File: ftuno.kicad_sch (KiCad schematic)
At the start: 63 parts, among them CN1 AFC10-S04QCA-00, J1 USB_C_Receptacle_USB2.0_16P, J10 Conn_01x10_Socket, J11 Conn_01x08_Pin, J12 Conn_01x08_Socket, J2 Conn_02x03_Odd_Even, J3 Conn_01x08_Pin, J4 Conn_01x08_Socket, J5 Conn_02x04_Odd_Even, J6 Conn_01x06_Pin, J7 Conn_01x06_Socket, J8 Conn_01x04_Socket, J9 Conn_01x10_Pin, Q1 AO3401, Q2 BSS138PS_C5224289, Q3 BSS138PS_C5224289, SW1 SK12D07VG4, SW2 SKHMQLE010, U1 CH340C, U2 TPS54302, U3 ME6217C33M5G, U4 ATmega328P-A, X1 CSTCE16M0V53-R0

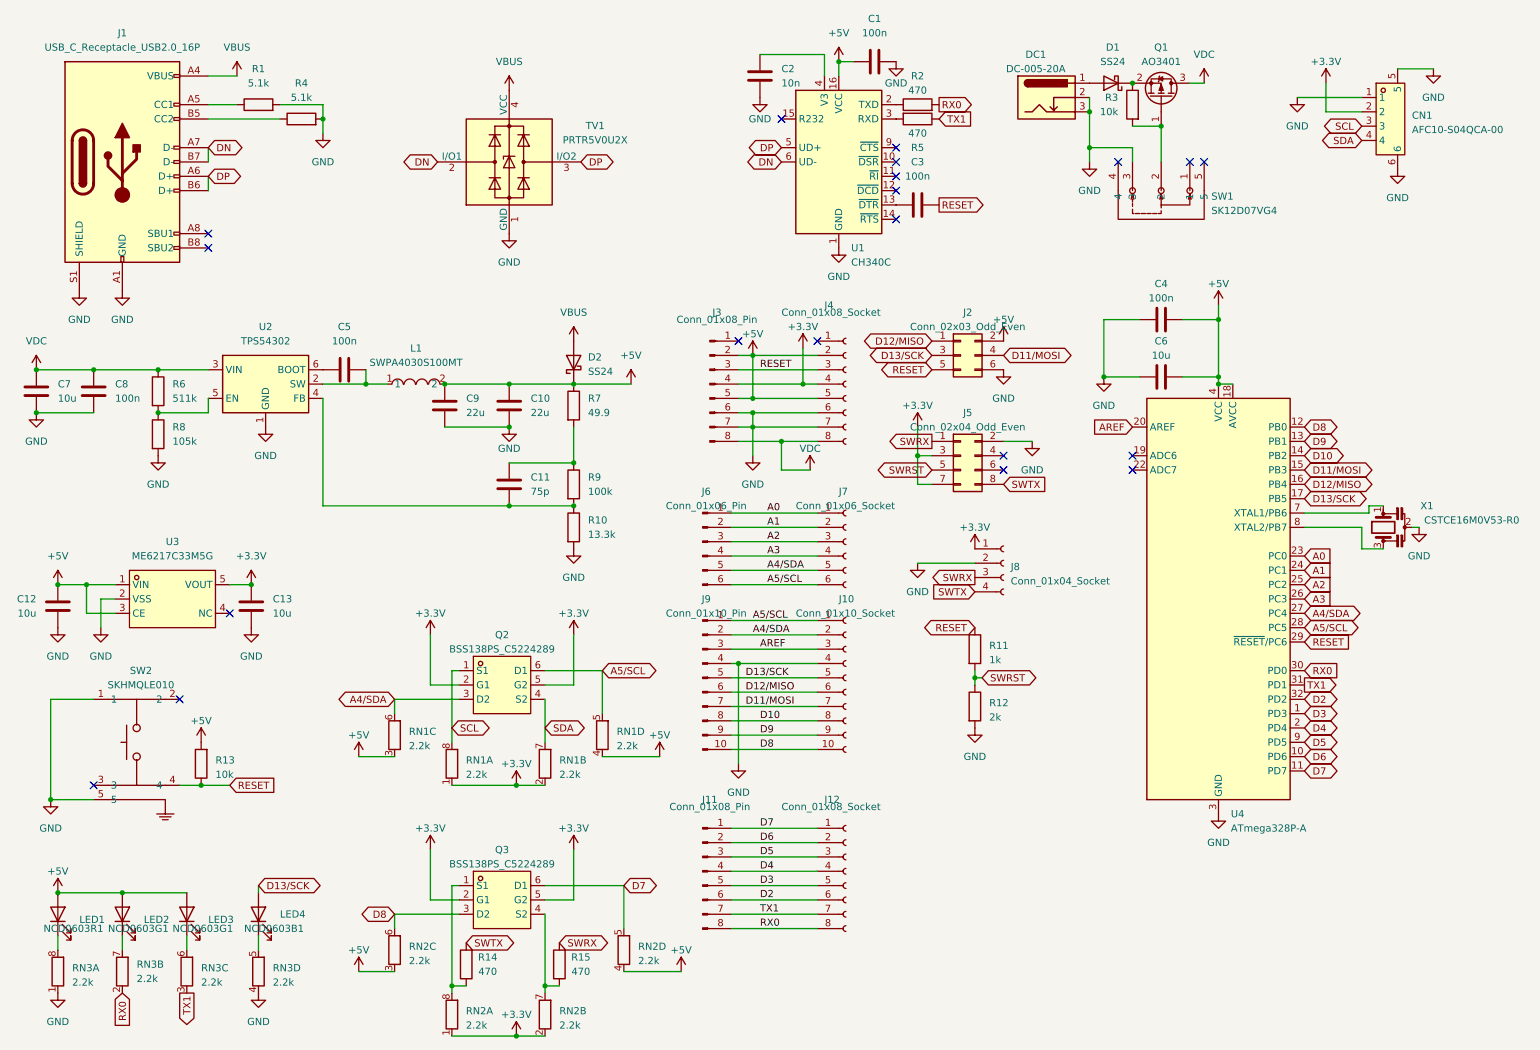
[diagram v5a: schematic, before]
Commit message: get rid of buck convertor and use LDO instead
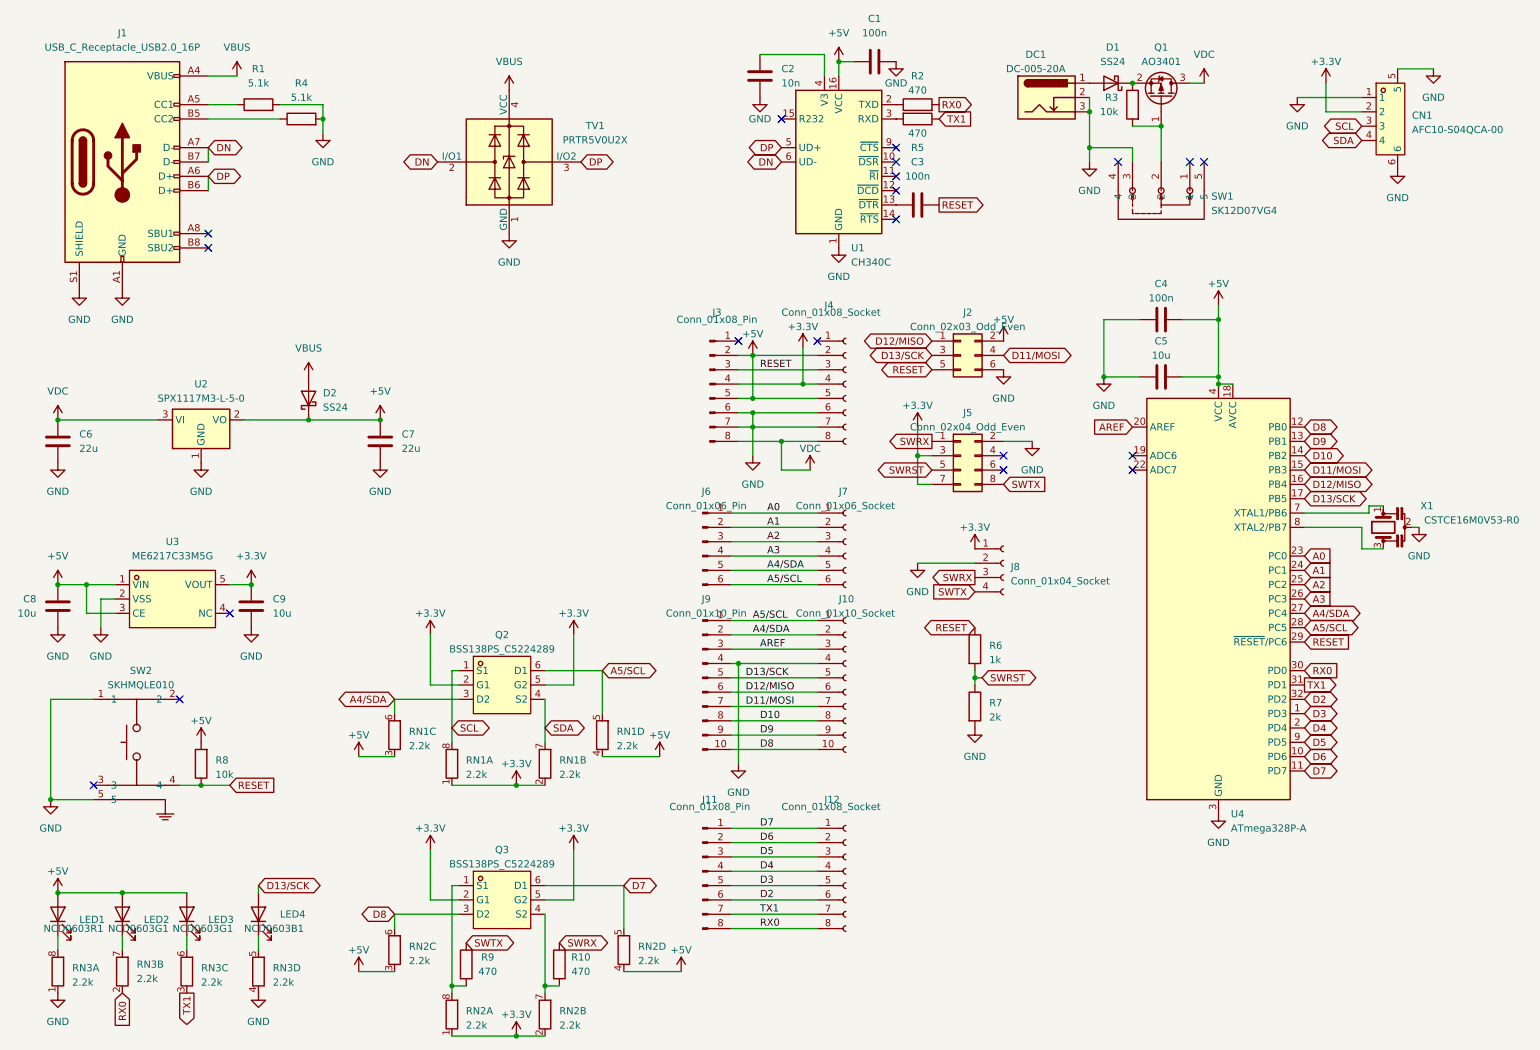
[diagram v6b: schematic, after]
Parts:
- removed C10: 22u, Capacitor_SMD:C_0805_2012Metric, symbol Device:C
- removed C11: 75p, Capacitor_SMD:C_0402_1005Metric, symbol Device:C
- removed C5, C8: 100n, Capacitor_SMD:C_0603_1608Metric, symbol Device:C
- removed C7: 10u, Capacitor_SMD:C_1206_3216Metric, symbol Device:C
- removed L1: SWPA4030S100MT, uno:IND-SMD_L4.0-W4.0, symbol uno:SWPA4030S100MT
- removed R10: 13.3k, Resistor_SMD:R_0603_1608Metric, symbol Device:R
- removed R6: 511k, Resistor_SMD:R_0402_1005Metric, symbol Device:R
- removed R7: 49.9, Resistor_SMD:R_0603_1608Metric, symbol Device:R
- removed R8: 105k, Resistor_SMD:R_0402_1005Metric, symbol Device:R
- removed R9: 100k, Resistor_SMD:R_0603_1608Metric, symbol Device:R
- removed U2: TPS54302, Package_TO_SOT_SMD:SOT-23-6, symbol Regulator_Switching:TPS54302
- added C6: 22u, Capacitor_SMD:C_0805_2012Metric, symbol Device:C
- added U2: SPX1117M3-L-5-0, Package_TO_SOT_SMD:SOT-223-3_TabPin2, symbol Regulator_Linear:AMS1117-5.0
- renumbered C6 to C5, C9 to C7, C12 to C8, C13 to C9, R15 to R10, R11 to R6, R12 to R7, R13 to R8, R14 to R9
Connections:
- net +5V: now also U2.2 (VO)
- net GND: now also C6.2, U2.1 (GND)
- net VDC: now also C6.1, U2.3 (VI)
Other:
- moved on the sheet: C7, D2

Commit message: fix qwiic pin arrangement, move usb conn
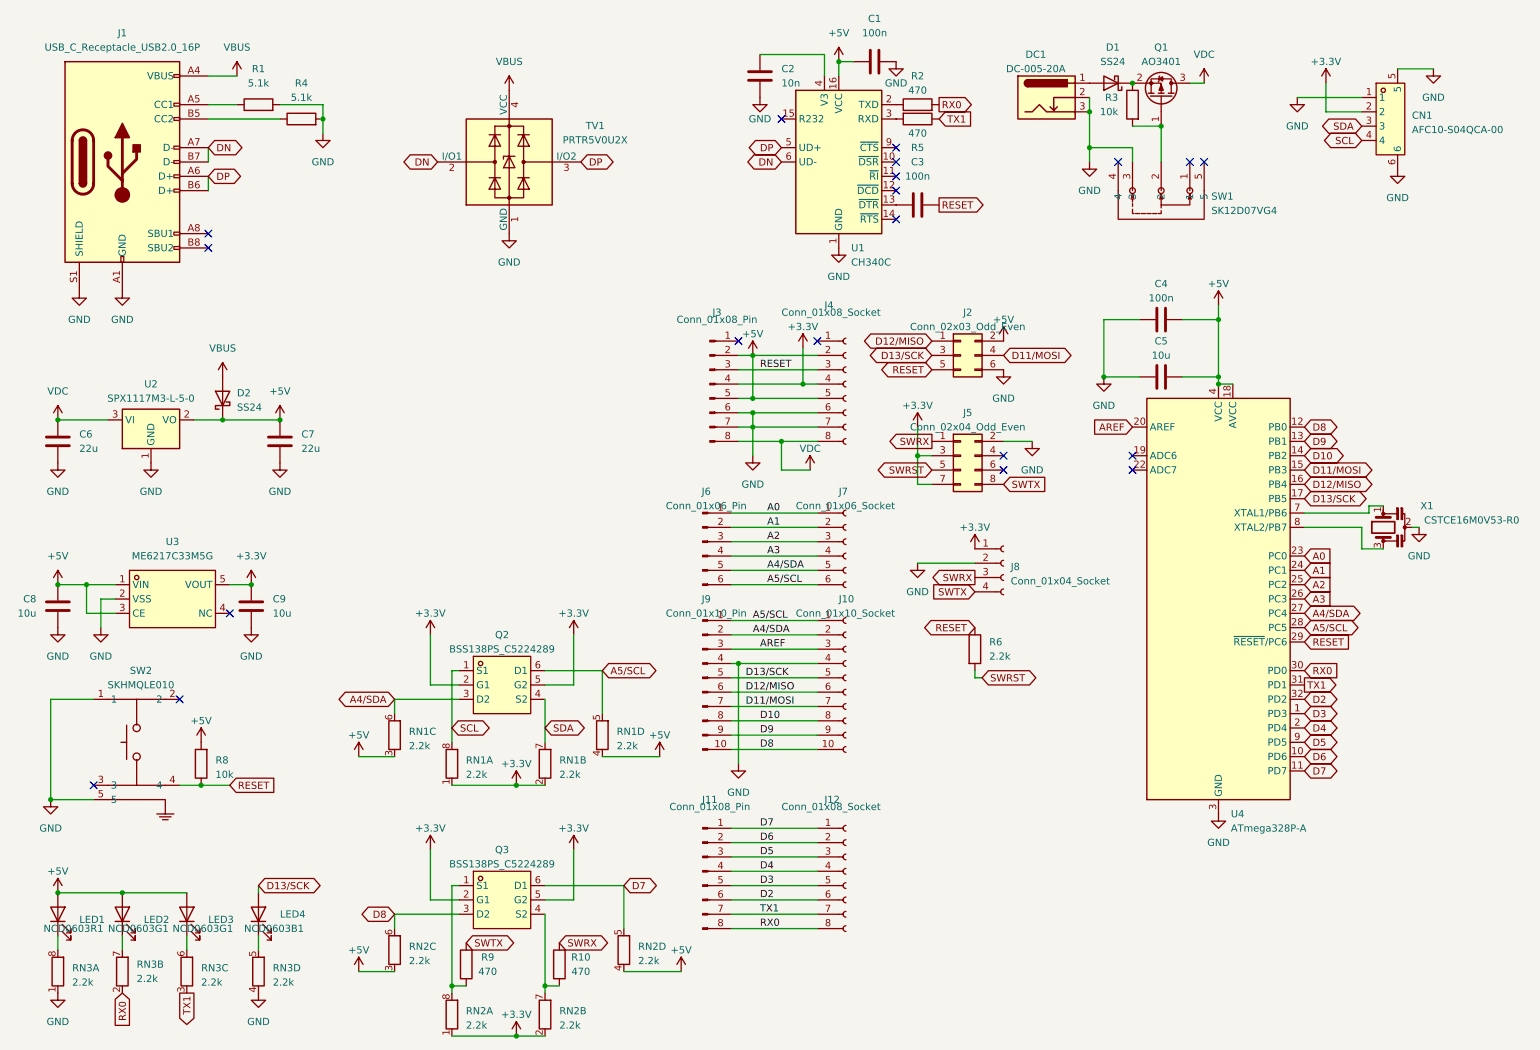
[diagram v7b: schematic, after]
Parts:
- removed R7: 2k, Resistor_SMD:R_0402_1005Metric, symbol Device:R
- R6: value 1k -> 2.2k
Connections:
- net SCL: now also CN1.4; no longer CN1.3
- net SDA: now also CN1.3; no longer CN1.4
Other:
- moved on the sheet: C7, D2, U2

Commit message: refine 1117 in and out
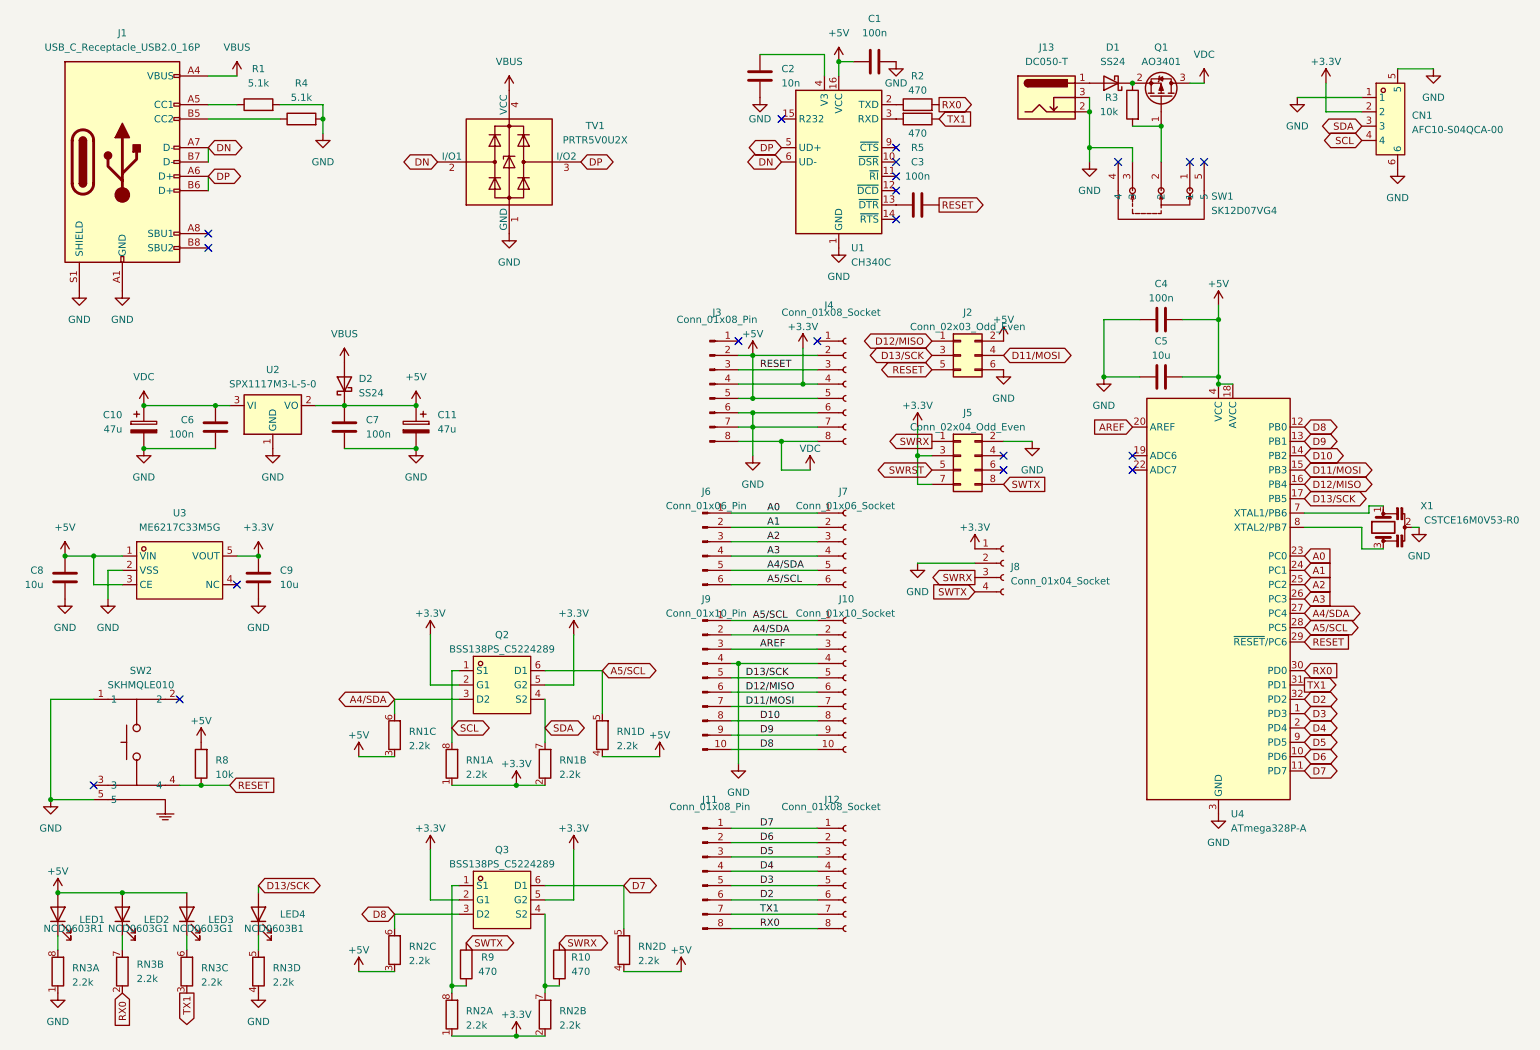
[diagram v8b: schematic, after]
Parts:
- removed DC1: DC-005-20A, uno:DC-IN-TH_DC-005-20A, symbol Connector:Barrel_Jack_Switch_Pin3Ring
- removed R6: 2.2k, Resistor_SMD:R_0402_1005Metric, symbol Device:R
- added C10, C11: 47u, Capacitor_SMD:CP_Elec_6.3x5.4, symbol Device:C_Polarized
- added J13: DC050-T, uno:DC-IN_DC050-T, symbol Connector:Barrel_Jack_Switch
- C6, C7: value 22u -> 100n; footprint Capacitor_SMD:C_0805_2012Metric -> Capacitor_SMD:C_0603_1608Metric
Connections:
- net +5V: now also C11.1
- net GND: now also C10.2, C11.2, J13.2, J13.3
- net VDC: now also C10.1
- net at D1.2 (A): now also J13.1
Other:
- moved on the sheet: C8, C9, D2, U2, U3
